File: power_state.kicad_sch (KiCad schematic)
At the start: 103 parts, among them Q101 BSZ018N04LS6, Q102 IQE013N04LM6, Q103 BSZ018N04LS6, Q104 IQE013N04LM6, Q105 GS2N7002KW, Q106 GS2N7002KW, U101 UCC27282DRC, U102 ACS37030LLZATR-040B3, U103 UCC27282DRC, U104 ACS37030LLZATR-040B3, U106 INA187A1IDBVR

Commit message: Updated Schematic v1.0
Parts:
- C116, C128: now left out of the parts list
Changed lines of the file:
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@@
 		(effects
 			(font
+				(face "Calibri")
 				(size 1.27 1.27)
-				(italic yes)
 				(color 0 0 0 1)
 			)
@@
 		(effects
 			(font
+				(face "Calibri")
 				(size 1.27 1.27)
-				(italic yes)
 				(color 0 0 0 1)
 			)
@@
 	(text "L_{par} = 1 / [ 2pi f_{1} C_{par} ]"
 		(exclude_from_sim no)
-		(at 165.1 276.86 0)
+		(at 166.37 276.86 0)
 		(effects
 			(font
+				(face "Calibri")
 				(size 1.27 1.27)
-				(italic yes)
 				(color 0 0 0 1)
 			)
@@
 	(text "C_{par} = C_{EXT} [ f_{2}^{2} / ( f_{1}^{2} - f_{2}^{2} ) ]"
 		(exclude_from_sim no)
-		(at 165.1 273.05 0)
+		(at 166.37 273.05 0)
 		(effects
 			(font
+				(face "Calibri")
 				(size 1.27 1.27)
-				(italic yes)
 				(color 0 0 0 1)
 			)
@@
 		(in_bom no)
 		(on_board yes)
-		(in_pos_files yes)
+		(in_pos_files no)
 		(dnp no)
 		(property "Reference" "NT103"
@@
 		(in_bom no)
 		(on_board yes)
-		(in_pos_files yes)
+		(in_pos_files no)
 		(dnp no)
 		(property "Reference" "NT102"
@@
 		(in_bom no)
 		(on_board yes)
-		(in_pos_files yes)
+		(in_pos_files no)
 		(dnp no)
 		(property "Reference" "NT105"
@@
 		(in_bom no)
 		(on_board yes)
-		(in_pos_files yes)
+		(in_pos_files no)
 		(dnp no)
 		(property "Reference" "NT101"
@@
 		(body_style 1)
 		(exclude_from_sim no)
-		(in_bom yes)
+		(in_bom no)
 		(on_board yes)
 		(in_pos_files yes)
@@
 		(body_style 1)
 		(exclude_from_sim no)
-		(in_bom yes)
+		(in_bom no)
 		(on_board yes)
 		(in_pos_files yes)

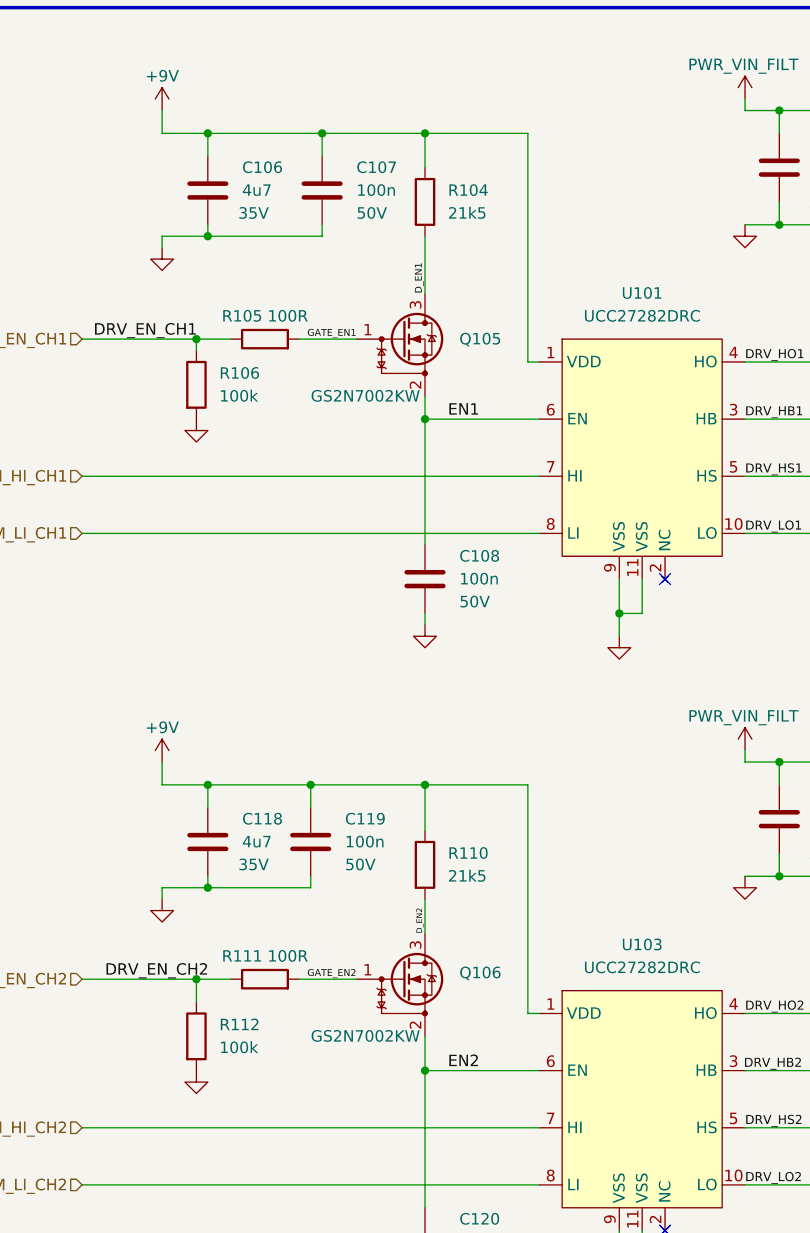
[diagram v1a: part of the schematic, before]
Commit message: Rev1.1
- Removed the Mosfet that Enable the ICs Gate Driver (p.1)
- Changed ADC input Capacitor 47pF to 1nF. (p.6
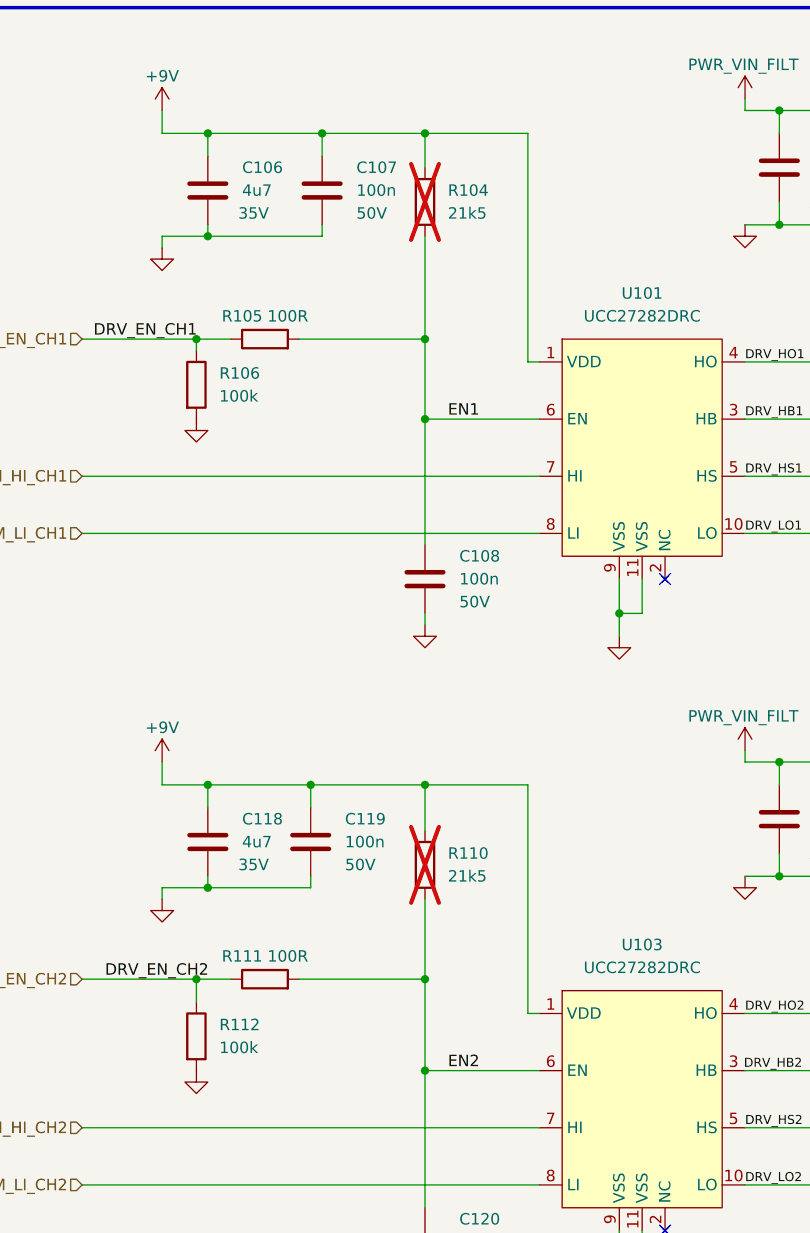
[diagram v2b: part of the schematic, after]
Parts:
- removed Q105, Q106: GS2N7002KW, 0_SOT:SOT-323_SC-70, symbol 0_mosfet:GS2N7002KW
- R104, R110: now not fitted
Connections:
- net D_EN1 is gone; now on net EN1: R104.1
- net D_EN2 is gone; now on net EN2: R110.2
- net GATE_EN1 is gone; now on net EN1: R105.2
- net GATE_EN2 is gone; now on net EN2: R111.2
